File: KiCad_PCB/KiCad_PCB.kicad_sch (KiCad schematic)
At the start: 33 parts, among them J1 Conn_01x04, J2 USB-C31-S-RA-CS2-SMT-BK-T{sla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, U1 LT3021ES8, U2 NRF52832-QFAA-R, Y1 ECS-320-8-33B-7KM-TR, Y2 ECS-.327-12.5-12R-TR

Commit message: PCB in progress
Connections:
- net +1V8: now also U2.36 (VDD2), U2.48 (VDD3)
- net GND: now also U2.49 (EXP), Y1.2 (GND_1); no longer Y1.3 (OUT/IN)
- net at U2.16 (P0.13): no longer R2.2
- net at U2.18 (P0.15): no longer D1.A
- net at L2.1, U2.30 (ANT): now also C10.1, E1.1, L2.2
- net at C5.2, U2.34 (XC1): now also Y1.3 (OUT/IN); no longer Y1.2 (GND_1)
- net at U2.38 (P0.26): now also D1.A
- net at U2.42 (P0.30): now also R2.2
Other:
- moved on the sheet: C10, D1, E1, R1, R2, S1

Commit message: Updated KiCad project
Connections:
- net at C10.1, L2.1, U2.30 (ANT): no longer E1.1, L2.2
- new net: E1.1, L2.2
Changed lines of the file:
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@@
   (junction (at 72.39 83.82) (diameter 0) (color 0 0 0 0)
   )
-  (junction (at 138.43 121.92) (diameter 0) (color 0 0 0 0)
-  )
   (junction (at 134.62 91.44) (diameter 0) (color 0 0 0 0)
   )
@@
   (junction (at 33.02 165.1) (diameter 0) (color 0 0 0 0)
   )
-  (junction (at 146.05 121.92) (diameter 0) (color 0 0 0 0)
-  )
   (junction (at 44.45 58.42) (diameter 0) (color 0 0 0 0)
   )
@@
   )
   (wire (pts (xy 127 114.3) (xy 129.54 114.3))
-    (stroke (width 0) (type default) (color 0 0 0 0))
-  )
-  (wire (pts (xy 146.05 121.92) (xy 138.43 121.92))
     (stroke (width 0) (type default) (color 0 0 0 0))
   )
@@
   )
   (symbol (lib_id "power:GND") (at 148.59 55.88 90) (unit 1)
-    (in_bom yes) (on_board yes) (fields_autoplaced)
+    (in_bom yes) (on_board yes)
     (property "Reference" "#PWR0115" (id 0) (at 154.94 55.88 0)
       (effects (font (size 1.27 1.27)) hide)
     )
-    (property "Value" "GND" (id 1) (at 152.4 55.8799 90)
+    (property "Value" "GND" (id 1) (at 152.4 55.88 90)
       (effects (font (size 1.27 1.27)) (justify right))
     )
@@
   )
   (symbol (lib_id "componentes:ECS-.327-12.5-12R-TR") (at 67.31 83.82 0) (unit 1)
-    (in_bom yes) (on_board yes) (fields_autoplaced)
-    (property "Reference" "Y2" (id 0) (at 67.31 76.2 0))
-    (property "Value" "ECS-.327-12.5-12R-TR" (id 1) (at 67.31 78.74 0))
+    (in_bom yes) (on_board yes)
+    (property "Reference" "Y2" (id 0) (at 67.31 77.47 0))
+    (property "Value" "ECS-.327-12.5-12R-TR" (id 1) (at 67.31 80.01 0))
     (property "Footprint" "componentes:XTAL_ECS-.327-12.5-12R-TR" (id 2) (at 67.31 83.82 0)
       (effects (font (size 1.27 1.27)) (justify left bottom) hide)
@@
   )
   (symbol (lib_id "power:GND") (at 148.59 60.96 90) (unit 1)
-    (in_bom yes) (on_board yes) (fields_autoplaced)
+    (in_bom yes) (on_board yes)
     (property "Reference" "#PWR0116" (id 0) (at 154.94 60.96 0)
       (effects (font (size 1.27 1.27)) hide)

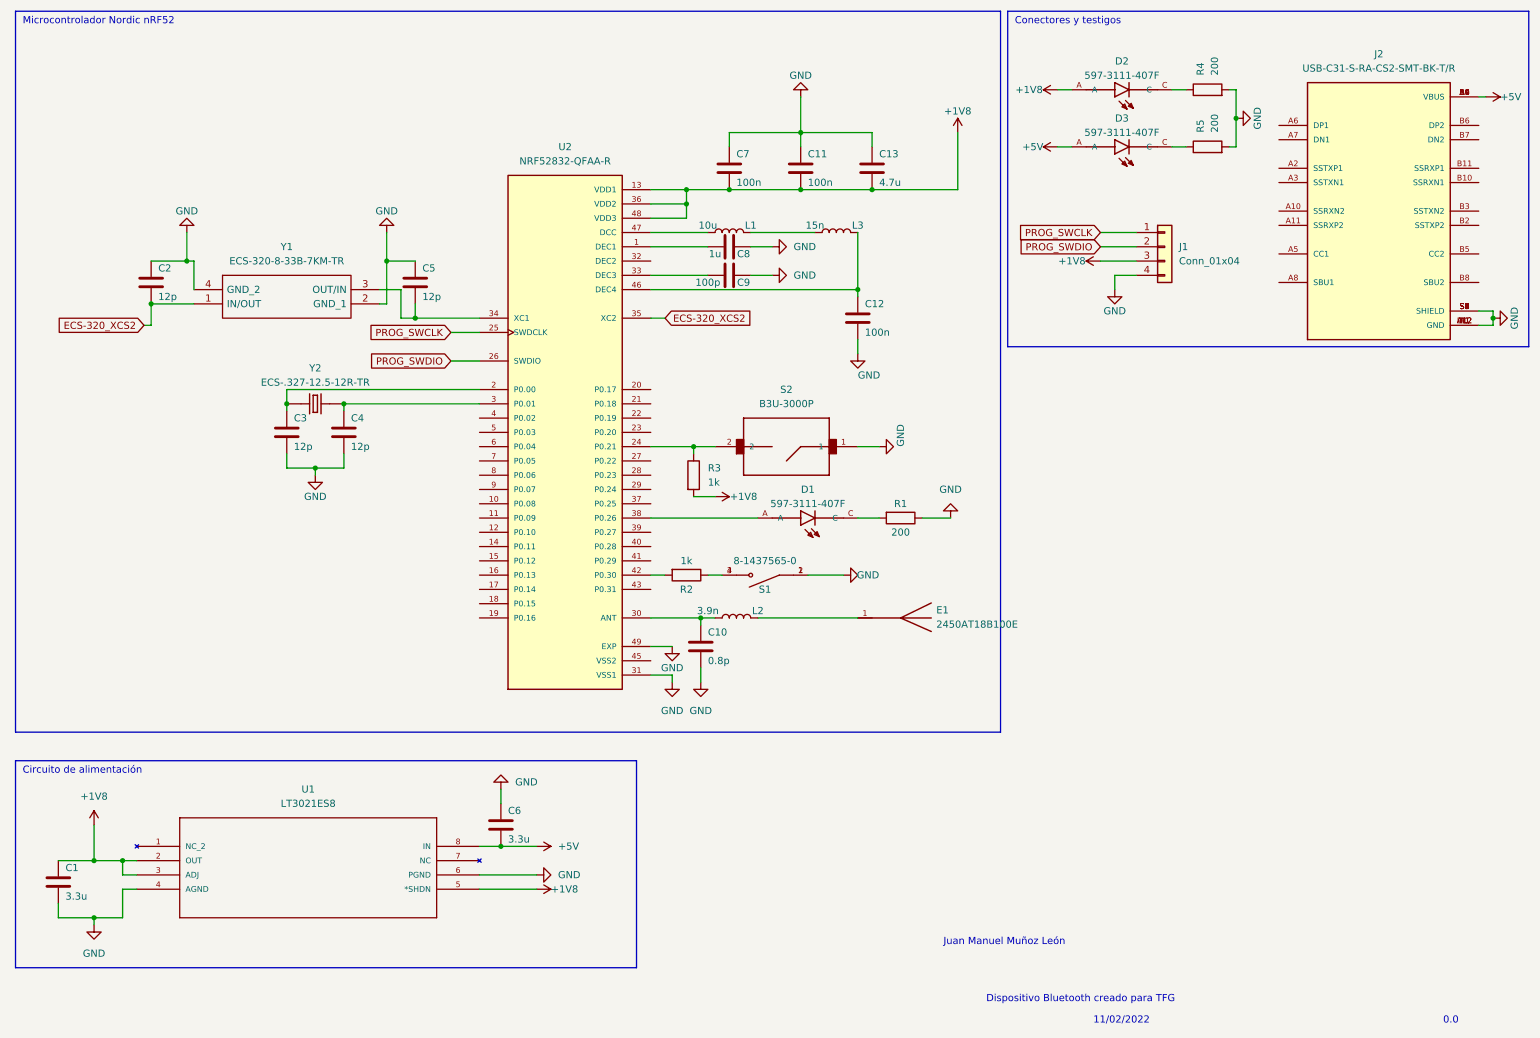
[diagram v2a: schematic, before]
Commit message: Updated footprints and added battery holder on KiCad project
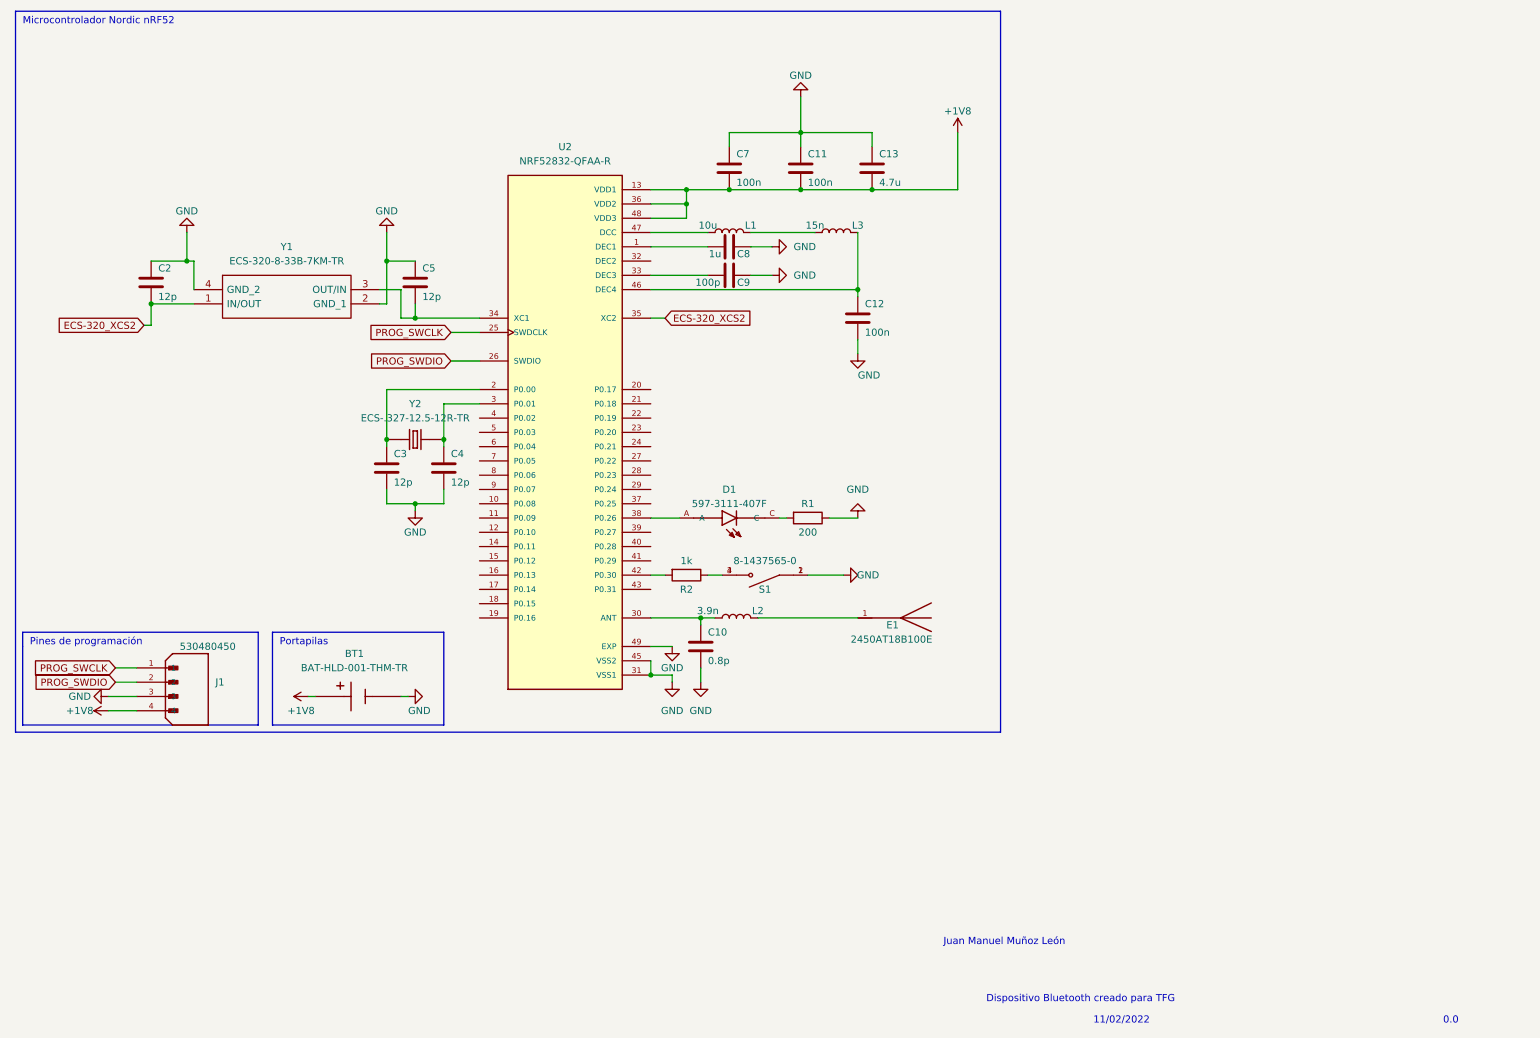
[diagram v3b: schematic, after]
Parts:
- removed C1, C6: 3.3u, Capacitor_SMD:C_0805_2012Metric, symbol Device:C
- removed D2, D3: 597-3111-407F, componentes:LEDC3216X110N, symbol componentes:597-3111-407F
- removed J1: Conn_01x04, Connector_PinHeader_2.54mm:PinHeader_1x04_P2.54mm_Vertical, symbol Connector_Generic:Conn_01x04
- removed J2: USB-C31-S-RA-CS2-SMT-BK-T/R, componentes:ADAM_USB-C31-S-RA-CS2-SMT-BK-T_R, symbol componentes:USB-C31-S-RA-CS2-SMT-BK-T{brace}slash}R
- removed R3: 1k, Resistor_SMD:R_0805_2012Metric, symbol Device:R
- removed R4, R5: 200, Resistor_SMD:R_0805_2012Metric, symbol Device:R
- removed S2: B3U-3000P, componentes:SW_B3U-3000P, symbol componentes:B3U-3000P
- removed U1: LT3021ES8, componentes:SO-8_S, symbol componentes:LT3021ES8
- added BT1: BAT-HLD-001-THM-TR, componentes:BAT_BAT-HLD-001-THM-TR, symbol componentes:BAT-HLD-001-THM-TR
- added J1: 530480450, componentes:MOLEX_530480450, symbol componentes:530480450
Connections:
- net +1V8: now also BT1.P1, BT1.P2, BT1.P3, BT1.P4, J1.4
- net GND: now also U2.45 (VSS2), BT1.N, J1.3
- net PROG_SWCLK: now also J1.1
- net PROG_SWDIO: now also J1.2
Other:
- note added: "Pines de programación"
- note added: "Portapilas"
- note removed: "Circuito de alimentación"
- note removed: "Conectores y testigos"
- moved on the sheet: C3, C4, D1, R1, Y2

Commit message: Tutorías 10/3
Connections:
- net GND: now also J1.1; no longer J1.3
- net PROG_SWCLK: now also J1.3; no longer J1.1
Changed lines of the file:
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@@
     )
   )
-  (global_label "PROG_SWCLK" (shape input) (at 31.75 130.81 180) (fields_autoplaced)
+  (global_label "PROG_SWCLK" (shape input) (at 30.48 135.89 180) (fields_autoplaced)
     (effects (font (size 1.27 1.27)) (justify right))
-    (property "Intersheet References" "${INTERSHEET_REFS}" (id 0) (at 16.9998 130.7306 0)
+    (property "Intersheet References" "${INTERSHEET_REFS}" (id 0) (at 15.7298 135.8106 0)
       (effects (font (size 1.27 1.27)) (justify right) hide)
     )
@@
     (pin "1")
   )
-  (symbol (lib_id "power:GND") (at 30.48 135.89 270) (unit 1)
-    (in_bom yes) (on_board yes)
-    (property "Reference" "#PWR0126" (id 0) (at 24.13 135.89 0)
-      (effects (font (size 1.27 1.27)) hide)
-    )
-    (property "Value" "GND" (id 1) (at 25.4 135.89 90))
-    (property "Footprint" "" (id 2) (at 30.48 135.89 0)
-      (effects (font (size 1.27 1.27)) hide)
-    )
-    (property "Datasheet" "" (id 3) (at 30.48 135.89 0)
-      (effects (font (size 1.27 1.27)) hide)
-    )
+  (symbol (lib_id "power:GND") (at 31.75 130.81 270) (unit 1)
+    (in_bom yes) (on_board yes)
+    (property "Reference" "#PWR0126" (id 0) (at 25.4 130.81 0)
+      (effects (font (size 1.27 1.27)) hide)
+    )
+    (property "Value" "GND" (id 1) (at 26.67 130.81 90))
+    (property "Footprint" "" (id 2) (at 31.75 130.81 0)
+      (effects (font (size 1.27 1.27)) hide)
+    )
+    (property "Datasheet" "" (id 3) (at 31.75 130.81 0)
+      (effects (font (size 1.27 1.27)) hide)
+    )

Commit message: Tutoría Modificacion PCB
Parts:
- C10, C11, C12, C13, C2, C3, C4, C5, C7, C8, C9: footprint Capacitor_SMD:C_0805_2012Metric -> Capacitor_SMD:C_0603_1608Metric
- R1, R2: footprint Resistor_SMD:R_0805_2012Metric -> Resistor_SMD:R_0603_1608Metric
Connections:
- net PROG_SWCLK: now also J1.2; no longer J1.3
- net PROG_SWDIO: now also J1.3; no longer J1.2
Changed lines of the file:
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@@
     )
   )
-  (global_label "PROG_SWCLK" (shape input) (at 30.48 135.89 180) (fields_autoplaced)
+  (global_label "PROG_SWCLK" (shape input) (at 31.75 133.35 180) (fields_autoplaced)
     (effects (font (size 1.27 1.27)) (justify right))
-    (property "Intersheet References" "${INTERSHEET_REFS}" (id 0) (at 15.7298 135.8106 0)
+    (property "Intersheet References" "${INTERSHEET_REFS}" (id 0) (at 16.9998 133.2706 0)
       (effects (font (size 1.27 1.27)) (justify right) hide)
     )
   )
-  (global_label "PROG_SWDIO" (shape input) (at 31.75 133.35 180) (fields_autoplaced)
+  (global_label "PROG_SWDIO" (shape input) (at 30.48 135.89 180) (fields_autoplaced)
     (effects (font (size 1.27 1.27)) (justify right))
-    (property "Intersheet References" "${INTERSHEET_REFS}" (id 0) (at 17.3626 133.2706 0)
+    (property "Intersheet References" "${INTERSHEET_REFS}" (id 0) (at 16.0926 135.8106 0)
       (effects (font (size 1.27 1.27)) (justify right) hide)
     )
@@
       (effects (font (size 1.27 1.27)) (justify left))
     )
-    (property "Footprint" "Capacitor_SMD:C_0805_2012Metric" (id 2) (at 164.7952 72.39 0)
+    (property "Footprint" "Capacitor_SMD:C_0603_1608Metric" (id 2) (at 164.7952 72.39 0)
       (effects (font (size 1.27 1.27)) hide)
     )
@@
     (property "Reference" "R1" (id 0) (at 154.94 101.6 90))
     (property "Value" "200" (id 1) (at 154.94 106.68 90))
-    (property "Footprint" "Resistor_SMD:R_0805_2012Metric" (id 2) (at 154.94 102.362 90)
+    (property "Footprint" "Resistor_SMD:R_0603_1608Metric" (id 2) (at 154.94 102.362 90)
       (effects (font (size 1.27 1.27)) hide)
     )
@@
       (effects (font (size 1.27 1.27)) (justify left))
     )
-    (property "Footprint" "Capacitor_SMD:C_0805_2012Metric" (id 2) (at 154.6352 45.72 0)
+    (property "Footprint" "Capacitor_SMD:C_0603_1608Metric" (id 2) (at 154.6352 45.72 0)
       (effects (font (size 1.27 1.27)) hide)
     )
@@
       (effects (font (size 1.27 1.27)) (justify left))
     )
-    (property "Footprint" "Capacitor_SMD:C_0805_2012Metric" (id 2) (at 141.9352 45.72 0)
+    (property "Footprint" "Capacitor_SMD:C_0603_1608Metric" (id 2) (at 141.9352 45.72 0)
       (effects (font (size 1.27 1.27)) hide)
     )
@@
     (property "Reference" "C9" (id 0) (at 143.51 62.23 90))
     (property "Value" "100p" (id 1) (at 137.16 62.23 90))
-    (property "Footprint" "Capacitor_SMD:C_0805_2012Metric" (id 2) (at 137.16 61.9252 0)
+    (property "Footprint" "Capacitor_SMD:C_0603_1608Metric" (id 2) (at 137.16 61.9252 0)
       (effects (font (size 1.27 1.27)) hide)
     )
@@
       (effects (font (size 1.27 1.27)) (justify left))
     )
-    (property "Footprint" "Capacitor_SMD:C_0805_2012Metric" (id 2) (at 80.9752 99.06 0)
+    (property "Footprint" "Capacitor_SMD:C_0603_1608Metric" (id 2) (at 80.9752 99.06 0)
       (effects (font (size 1.27 1.27)) hide)
     )
@@
       (effects (font (size 1.27 1.27)) (justify left))
     )
-    (property "Footprint" "Capacitor_SMD:C_0805_2012Metric" (id 2) (at 39.0652 66.04 0)
+    (property "Footprint" "Capacitor_SMD:C_0603_1608Metric" (id 2) (at 39.0652 66.04 0)
       (effects (font (size 1.27 1.27)) hide)
     )
@@
       (effects (font (size 1.27 1.27)) (justify left))
     )
-    (property "Footprint" "Capacitor_SMD:C_0805_2012Metric" (id 2) (at 136.8552 130.81 0)
+    (property "Footprint" "Capacitor_SMD:C_0603_1608Metric" (id 2) (at 136.8552 130.81 0)
       (effects (font (size 1.27 1.27)) hide)
     )
@@
       (effects (font (size 1.27 1.27)) (justify left))
     )
-    (property "Footprint" "Capacitor_SMD:C_0805_2012Metric" (id 2) (at 167.3352 45.72 0)
+    (property "Footprint" "Capacitor_SMD:C_0603_1608Metric" (id 2) (at 167.3352 45.72 0)
       (effects (font (size 1.27 1.27)) hide)
     )
@@
     (property "Reference" "R2" (id 0) (at 133.35 116.84 90))
     (property "Value" "1k" (id 1) (at 133.35 111.76 90))
-    (property "Footprint" "Resistor_SMD:R_0805_2012Metric" (id 2) (at 133.35 112.522 90)
+    (property "Footprint" "Resistor_SMD:R_0603_1608Metric" (id 2) (at 133.35 112.522 90)
       (effects (font (size 1.27 1.27)) hide)
     )
@@
       (effects (font (size 1.27 1.27)) (justify left))
     )
-    (property "Footprint" "Capacitor_SMD:C_0805_2012Metric" (id 2) (at 91.1352 99.06 0)
+    (property "Footprint" "Capacitor_SMD:C_0603_1608Metric" (id 2) (at 91.1352 99.06 0)
       (effects (font (size 1.27 1.27)) hide)
     )
@@
       (effects (font (size 1.27 1.27)) (justify left))
     )
-    (property "Footprint" "Capacitor_SMD:C_0805_2012Metric" (id 2) (at 86.0552 66.04 0)
+    (property "Footprint" "Capacitor_SMD:C_0603_1608Metric" (id 2) (at 86.0552 66.04 0)
       (effects (font (size 1.27 1.27)) hide)
     )
@@
     (property "Reference" "C8" (id 0) (at 143.51 57.15 90))
     (property "Value" "1u" (id 1) (at 138.43 57.15 90))
-    (property "Footprint" "Capacitor_SMD:C_0805_2012Metric" (id 2) (at 137.16 56.8452 0)
+    (property "Footprint" "Capacitor_SMD:C_0603_1608Metric" (id 2) (at 137.16 56.8452 0)
       (effects (font (size 1.27 1.27)) hide)
     )
@@
     )
     (path "/8dc8b5f4-3130-46f4-9c7a-f7056b01dba7"
-      (reference "C2") (unit 1) (value "12p") (footprint "Capacitor_SMD:C_0805_2012Metric")
+      (reference "C2") (unit 1) (value "12p") (footprint "Capacitor_SMD:C_0603_1608Metric")
     )
     (path "/7f1d1afb-649d-4e75-a6b0-5a12cc0a86b8"
-      (reference "C3") (unit 1) (value "12p") (footprint "Capacitor_SMD:C_0805_2012Metric")
+      (reference "C3") (unit 1) (value "12p") (footprint "Capacitor_SMD:C_0603_1608Metric")
     )
     (path "/ba599e5b-50c5-444c-9620-62d56953ce7f"
-      (reference "C4") (unit 1) (value "12p") (footprint "Capacitor_SMD:C_0805_2012Metric")
+      (reference "C4") (unit 1) (value "12p") (footprint "Capacitor_SMD:C_0603_1608Metric")
     )
     (path "/dff3df46-3737-4f7f-a92d-dac2e8871a38"
-      (reference "C5") (unit 1) (value "12p") (footprint "Capacitor_SMD:C_0805_2012Metric")
+      (reference "C5") (unit 1) (value "12p") (footprint "Capacitor_SMD:C_0603_1608Metric")
     )
     (path "/5f4a8894-09c6-4bec-a920-12fe09ca2f55"
-      (reference "C7") (unit 1) (value "100n") (footprint "Capacitor_SMD:C_0805_2012Metric")
+      (reference "C7") (unit 1) (value "100n") (footprint "Capacitor_SMD:C_0603_1608Metric")
     )
     (path "/fca302d0-5c39-47d5-951d-6afa996677a8"
-      (reference "C8") (unit 1) (value "1u") (footprint "Capacitor_SMD:C_0805_2012Metric")
+      (reference "C8") (unit 1) (value "1u") (footprint "Capacitor_SMD:C_0603_1608Metric")
     )
     (path "/608f4001-cff0-46a4-9e8b-63808992aebd"
-      (reference "C9") (unit 1) (value "100p") (footprint "Capacitor_SMD:C_0805_2012Metric")
+      (reference "C9") (unit 1) (value "100p") (footprint "Capacitor_SMD:C_0603_1608Metric")
     )
     (path "/9139e421-b12e-44d5-9237-37af176cd04c"
-      (reference "C10") (unit 1) (value "0.8p") (footprint "Capacitor_SMD:C_0805_2012Metric")
+      (reference "C10") (unit 1) (value "0.8p") (footprint "Capacitor_SMD:C_0603_1608Metric")
     )
     (path "/3c2d2407-2d0c-43bf-9e3d-902b2301426d"
-      (reference "C11") (unit 1) (value "100n") (footprint "Capacitor_SMD:C_0805_2012Metric")
+      (reference "C11") (unit 1) (value "100n") (footprint "Capacitor_SMD:C_0603_1608Metric")
     )
     (path "/0260649a-7e67-4013-a002-9f21265819c7"
-      (reference "C12") (unit 1) (value "100n") (footprint "Capacitor_SMD:C_0805_2012Metric")
+      (reference "C12") (unit 1) (value "100n") (footprint "Capacitor_SMD:C_0603_1608Metric")
     )
     (path "/b41f8a35-424f-4b31-ab71-32800b35b178"
-      (reference "C13") (unit 1) (value "4.7u") (footprint "Capacitor_SMD:C_0805_2012Metric")
+      (reference "C13") (unit 1) (value "4.7u") (footprint "Capacitor_SMD:C_0603_1608Metric")
     )
     (path "/e7837bba-4604-456b-811e-2fbdc4b80544"
@@
     )
     (path "/1d82de6f-ea2b-470a-b75b-09ec0eebcaf1"
-      (reference "R1") (unit 1) (value "200") (footprint "Resistor_SMD:R_0805_2012Metric")
+      (reference "R1") (unit 1) (value "200") (footprint "Resistor_SMD:R_0603_1608Metric")
     )
     (path "/b5190e10-ff79-4359-87b1-0c28e176c29f"
-      (reference "R2") (unit 1) (value "1k") (footprint "Resistor_SMD:R_0805_2012Metric")
+      (reference "R2") (unit 1) (value "1k") (footprint "Resistor_SMD:R_0603_1608Metric")
     )
     (path "/f166b3d3-4633-405d-8711-cb5cdc0e7abc"
